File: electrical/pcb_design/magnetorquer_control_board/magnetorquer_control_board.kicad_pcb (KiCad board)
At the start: 4 copper layers, 77 x 96 mm, 77 parts, among them J1 STLINK, J3 Molex_504050-1291, J4 External Power, J5 Molex_504050-1291, J6 Molex_504050-0891, J7 Molex_504050-0891, J8 Molex_504050-0491, U1 STM32L452RCT6, U2 BMI323, U3 BMI323, U4 TCAN330DR, U5 INA260, U6 TLV76733DRVx

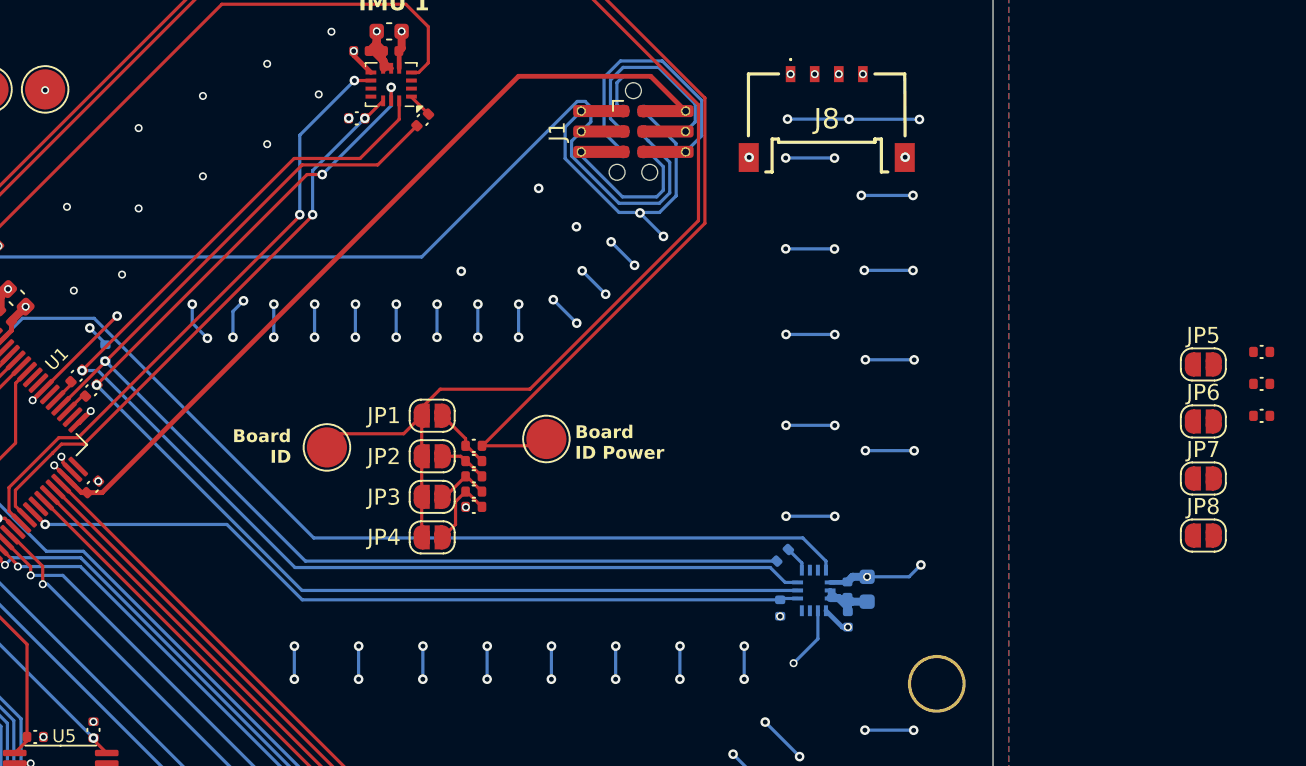
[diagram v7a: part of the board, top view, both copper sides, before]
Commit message: Laid out board id resistors and jumpers.
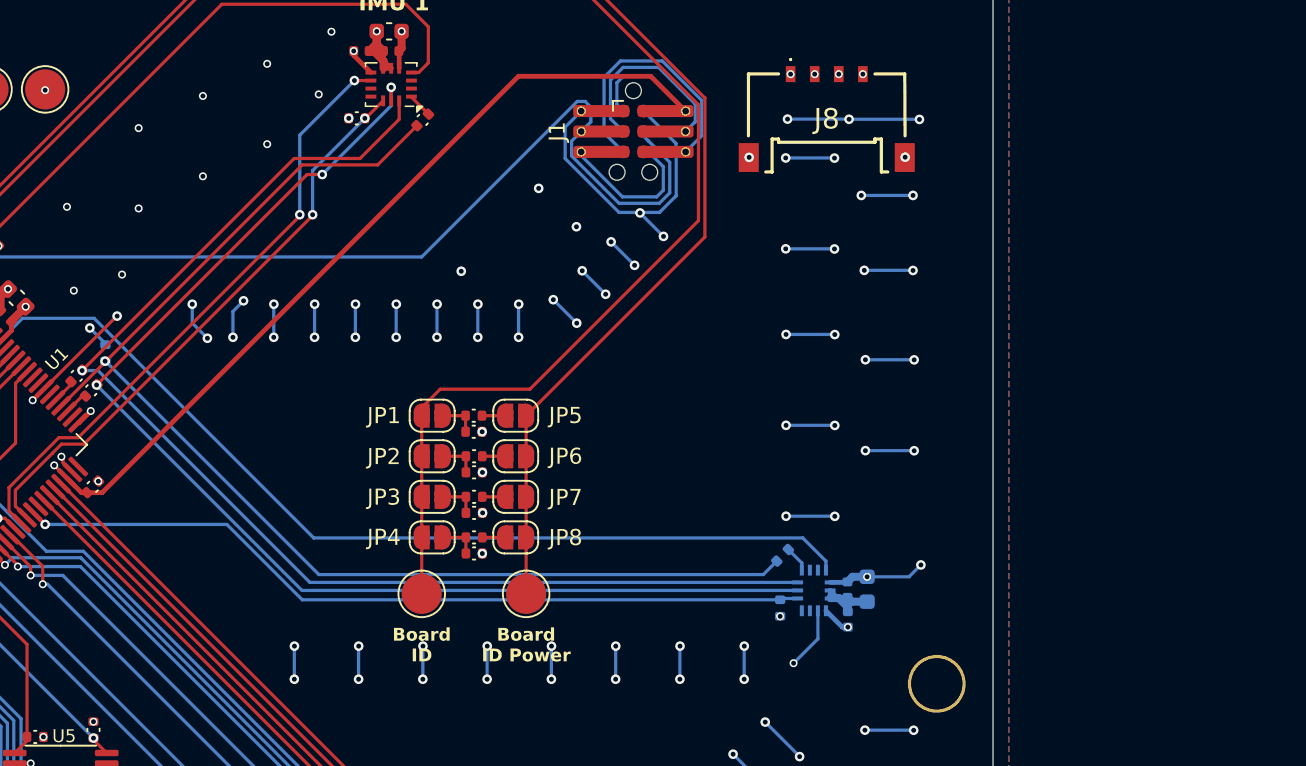
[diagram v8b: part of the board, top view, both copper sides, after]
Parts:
- moved R25 50.1 mm to (160.1, 90.0), turned to 180 degrees
- moved R24 50.0 mm to (160.1, 87.5), turned to 180 degrees
- moved R26 49.6 mm to (160.1, 89.0)
- moved JP5 42.9 mm to (162.7, 81.5), turned to 180 degrees
- moved JP6 42.9 mm to (162.7, 84.0), turned to 180 degrees
- moved JP7 42.8 mm to (162.7, 86.5), turned to 180 degrees
- moved JP8 42.8 mm to (162.7, 89.0), turned to 180 degrees
- moved TP8 10.9 mm to (156.9, 92.5)
- moved TP7 9.72 mm to (163.4, 92.5)
- moved R11 1.88 mm to (160.1, 81.5)
- moved R12 1.83 mm to (160.1, 82.5), turned to 0 degrees
- moved R13 1.25 mm to (160.1, 84.0)
- moved R14 1.20 mm to (160.1, 85.0), turned to 0 degrees
- moved R15 0.63 mm to (160.1, 86.5)
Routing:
- net BOARD_ID_PWR: track 113.7 -> 117.6 mm
- net BOARD_ID_SENS: track 121.7 -> 118.5 mm
- net Net-(JP4-B): track 4.79 -> 2.45 mm
- net Net-(JP5-B): track 0.00 -> 1.45 mm
- net Net-(JP8-B): track 0.00 -> 1.43 mm
- net Net-(JP7-B): track 0.00 -> 1.43 mm
- net Net-(JP6-B): track 0.00 -> 1.43 mm
- net Net-(JP1-B): track 3.81 -> 2.43 mm
- net Net-(JP3-B): track 3.15 -> 2.45 mm, vias 1 -> 0
- net SPI3_MISO: track 76.3 -> 77.0 mm
- net GND: vias 86 -> 90
